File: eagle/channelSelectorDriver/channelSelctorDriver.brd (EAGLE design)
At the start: 10 parts, among them IC1 4025N, IC2 4071N, IC3 4071N

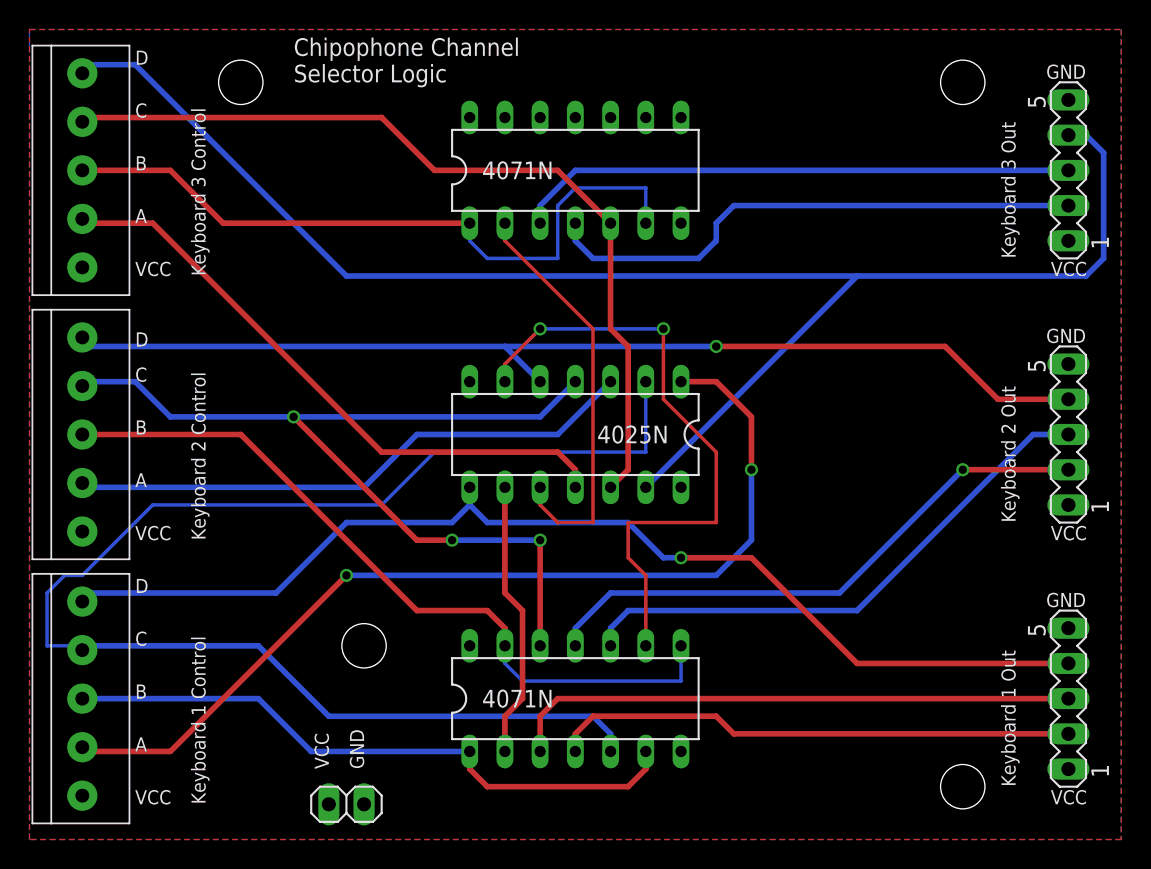
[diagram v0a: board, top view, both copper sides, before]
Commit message: Added a board outline so the edges of the selector driver don't get cut off
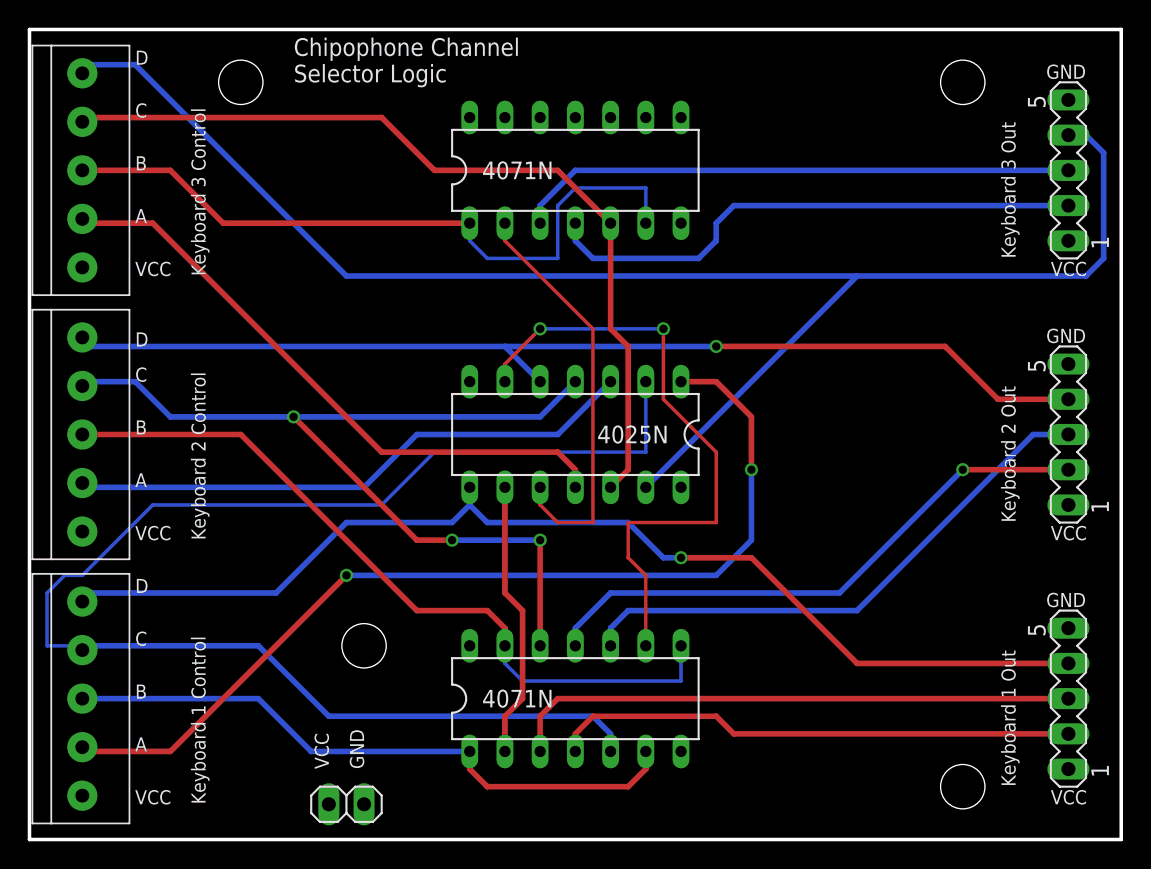
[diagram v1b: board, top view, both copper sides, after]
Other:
- board outline added: 78.7 x 58.4 mm
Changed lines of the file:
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@@
 <layer number="27" name="tValues" color="7" fill="1" visible="yes" active="yes"/>
 <layer number="28" name="bValues" color="7" fill="1" visible="yes" active="yes"/>
-<layer number="29" name="tStop" color="7" fill="3" visible="no" active="yes"/>
-<layer number="30" name="bStop" color="7" fill="6" visible="no" active="yes"/>
-<layer number="31" name="tCream" color="7" fill="4" visible="no" active="yes"/>
-<layer number="32" name="bCream" color="7" fill="5" visible="no" active="yes"/>
-<layer number="33" name="tFinish" color="6" fill="3" visible="no" active="yes"/>
-<layer number="34" name="bFinish" color="6" fill="6" visible="no" active="yes"/>
-<layer number="35" name="tGlue" color="7" fill="4" visible="no" active="yes"/>
-<layer number="36" name="bGlue" color="7" fill="5" visible="no" active="yes"/>
-<layer number="37" name="tTest" color="7" fill="1" visible="no" active="yes"/>
-<layer number="38" name="bTest" color="7" fill="1" visible="no" active="yes"/>
+<layer number="29" name="tStop" color="7" fill="3" visible="yes" active="yes"/>
+<layer number="30" name="bStop" color="7" fill="6" visible="yes" active="yes"/>
+<layer number="31" name="tCream" color="7" fill="4" visible="yes" active="yes"/>
+<layer number="32" name="bCream" color="7" fill="5" visible="yes" active="yes"/>
+<layer number="33" name="tFinish" color="6" fill="3" visible="yes" active="yes"/>
+<layer number="34" name="bFinish" color="6" fill="6" visible="yes" active="yes"/>
+<layer number="35" name="tGlue" color="7" fill="4" visible="yes" active="yes"/>
+<layer number="36" name="bGlue" color="7" fill="5" visible="yes" active="yes"/>
+<layer number="37" name="tTest" color="7" fill="1" visible="yes" active="yes"/>
+<layer number="38" name="bTest" color="7" fill="1" visible="yes" active="yes"/>
 <layer number="39" name="tKeepout" color="4" fill="11" visible="yes" active="yes"/>
 <layer number="40" name="bKeepout" color="1" fill="11" visible="yes" active="yes"/>
@@
 <layer number="42" name="bRestrict" color="1" fill="10" visible="yes" active="yes"/>
 <layer number="43" name="vRestrict" color="2" fill="10" visible="yes" active="yes"/>
-<layer number="44" name="Drills" color="7" fill="1" visible="no" active="yes"/>
+<layer number="44" name="Drills" color="7" fill="1" visible="yes" active="yes"/>
 <layer number="45" name="Holes" color="7" fill="1" visible="yes" active="yes"/>
-<layer number="46" name="Milling" color="3" fill="1" visible="no" active="yes"/>
-<layer number="47" name="Measures" color="7" fill="1" visible="no" active="yes"/>
+<layer number="46" name="Milling" color="3" fill="1" visible="yes" active="yes"/>
+<layer number="47" name="Measures" color="7" fill="1" visible="yes" active="yes"/>
 <layer number="48" name="Document" color="7" fill="1" visible="yes" active="yes"/>
 <layer number="49" name="Reference" color="7" fill="1" visible="yes" active="yes"/>
@@
 <text x="7.62" y="35.56" size="1.016" layer="21">D</text>
 <text x="7.62" y="17.78" size="1.016" layer="21">D</text>
+<wire x1="0" y1="58.42" x2="0" y2="0" width="0.254" layer="20"/>
+<wire x1="0" y1="0" x2="78.74" y2="0" width="0.254" layer="20"/>
+<wire x1="78.74" y1="0" x2="78.74" y2="58.42" width="0.254" layer="20"/>
+<wire x1="78.74" y1="58.42" x2="0" y2="58.42" width="0.254" layer="20"/>
 </plain>
 <attributes>

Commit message: Halved the size of the board. Much smaller, much cheaper.
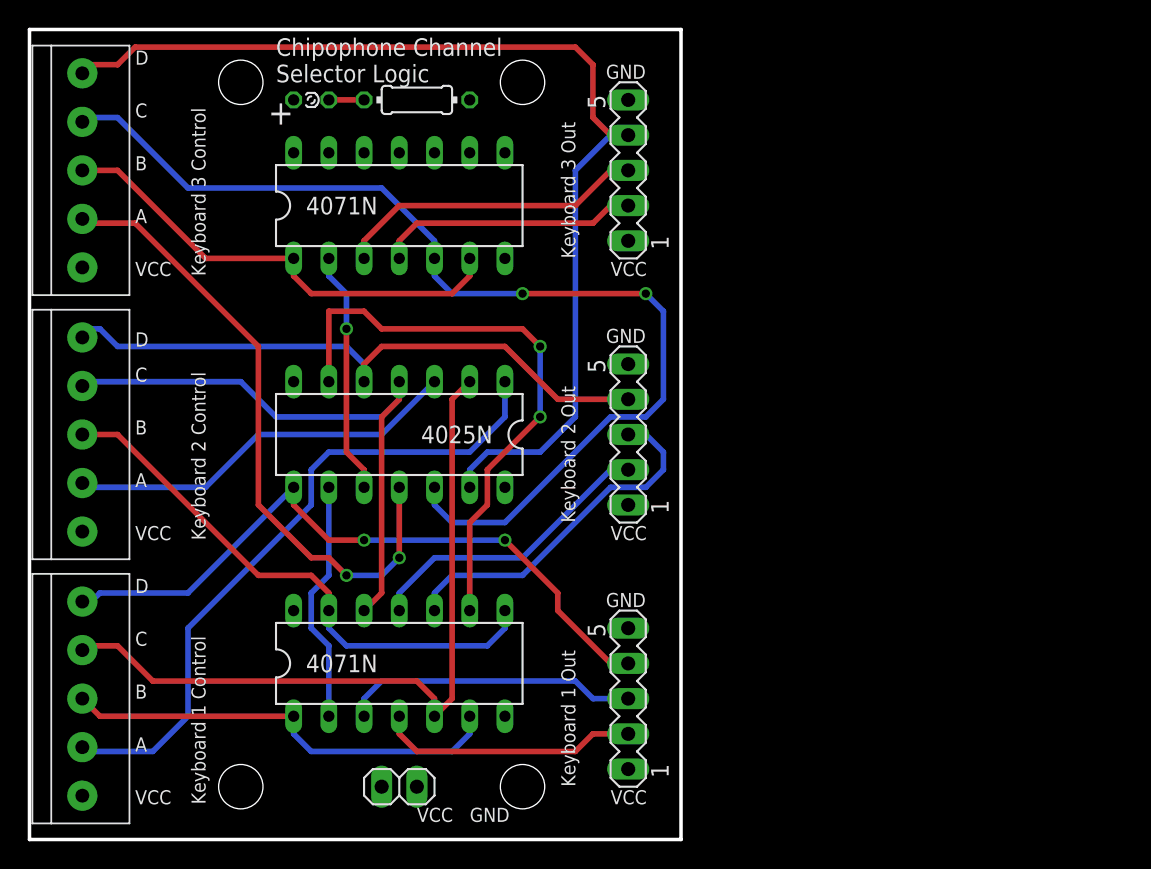
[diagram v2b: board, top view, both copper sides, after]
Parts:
- added LED1: (no value), led:LSU260
- added R1: (no value), resistor:0204/7
- moved FTPDL_S 31.8 mm to (43.2, 48.3)
- moved KBD1_S 31.8 mm to (43.2, 10.2)
- moved KBD2_S 31.8 mm to (43.2, 29.2)
- moved IC2 13.0 mm to (26.7, 45.7)
- moved IC3 13.0 mm to (26.7, 12.7)
- moved IC1 12.7 mm to (26.7, 29.2)
- moved JP1 4.02 mm to (26.7, 3.81)
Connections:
- new net N$12: LED1.K, R1.2
- net GND: now also R1.1
- net VCC: now also LED1.A
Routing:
- net N$5: track 101.1 -> 53.4 mm
- net N$18: track 113.4 -> 77.9 mm
- net N$4: track 76.9 -> 45.1 mm, vias 1 -> 0
- net N$23: track 80.4 -> 49.8 mm, vias 1 -> 2
- net N$17: track 67.1 -> 43.3 mm, vias 3 -> 0
- net N$10: track 69.9 -> 48.2 mm, vias 2 -> 0
- net N$20: track 39.7 -> 18.8 mm
- net N$13: track 41.6 -> 21.5 mm, vias 1 -> 0
- net N$9: track 41.2 -> 21.4 mm
- net N$8: track 37.9 -> 18.8 mm
- net N$21: track 40.4 -> 22.4 mm
- net N$19: track 50.9 -> 34.2 mm
- net N$6: track 61.7 -> 77.5 mm, vias 0 -> 2
- net N$15: track 54.6 -> 40.1 mm
- net N$14: track 40.1 -> 25.8 mm
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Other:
- board size 78.7 x 58.4 mm -> 47 x 58.4 mm
- board text added: "+"
